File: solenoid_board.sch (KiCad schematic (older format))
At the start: 38 parts, among them J1 Screw_Terminal_01x02, J10 Screw_Terminal_01x02, J11 Screw_Terminal_01x02, J12 Screw_Terminal_01x06, J13 Conn_01x01_Male, J14 Screw_Terminal_01x06, J2 MCU_LEFT_LEGS, J3 MCU_RIGHT_LEGS, J4 RJ45, J5 RJ45, J6 Screw_Terminal_01x06, J7 Screw_Terminal_01x02, J8 Screw_Terminal_01x02, J9 Screw_Terminal_01x02, Q1 PHP79NQ08LT, Q2 PHP79NQ08LT, Q3 PHP79NQ08LT, Q4 PHP79NQ08LT, Q5 PHP79NQ08LT, Q6 PHP79NQ08LT, U1 CDSOT23-SM712, U4 SN65HVD72DR, U5 74HC165, U6 74HC165

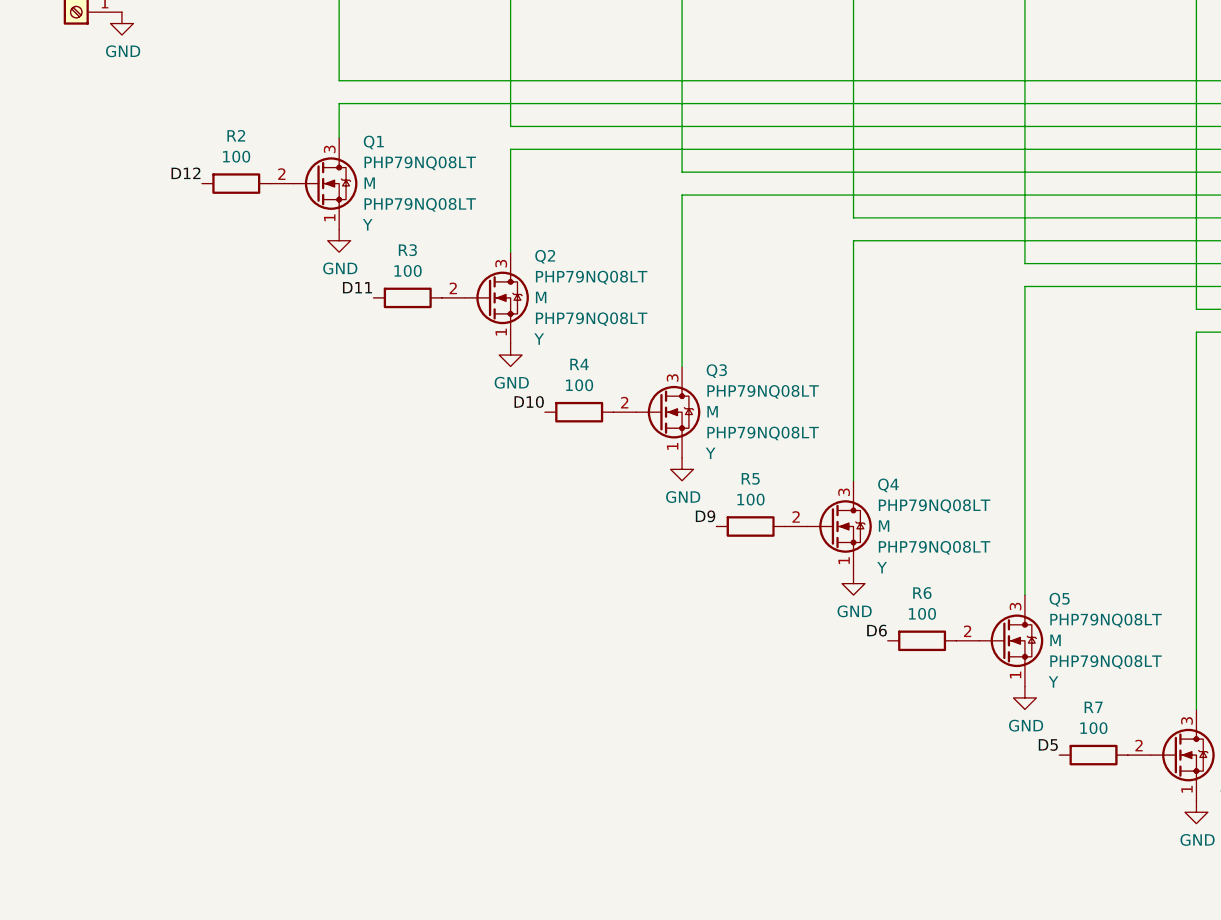
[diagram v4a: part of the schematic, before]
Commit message: Laid about half the wire. Next Step, lay out the wires for the digital electronics
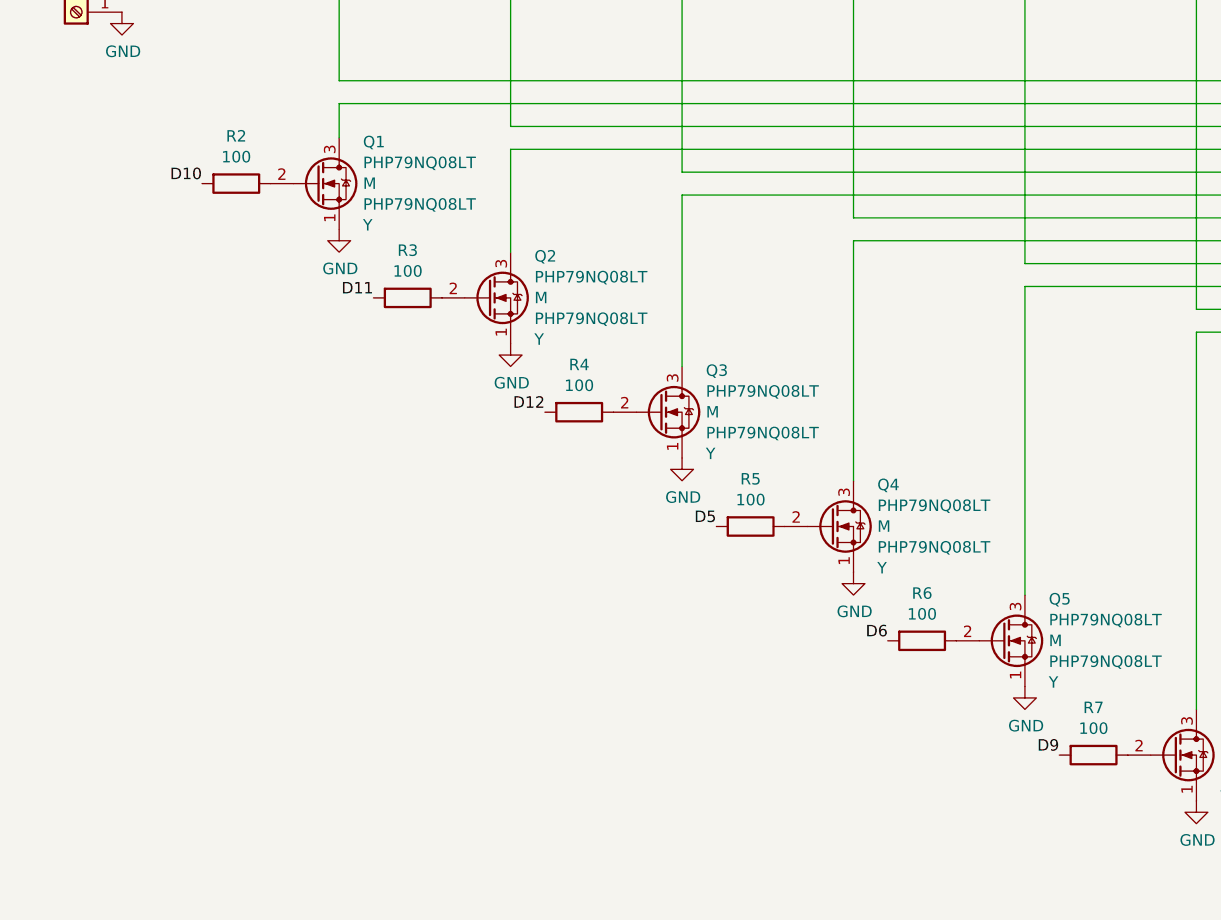
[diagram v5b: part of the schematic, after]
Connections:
- net D10: now also R2.2; no longer R4.2
- net D12: now also R4.2; no longer R2.2
- net D5: now also R5.2; no longer R7.2
- net D9: now also R7.2; no longer R5.2
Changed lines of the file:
@@
 $EndComp
 Text Label 5150 1900 2    50   ~ 0
-D12
+D10
 $Comp
 L MOSFETs:PHP79NQ08LT Q1
@@
 D11
 Text Label 6650 2900 2    50   ~ 0
-D10
+D12
 Text Label 7400 3400 2    50   ~ 0
-D9
+D5
 Text Label 8150 3900 2    50   ~ 0
 D6
 Text Label 8900 4400 2    50   ~ 0
-D5
+D9
 Text Label 1250 6250 0    50   ~ 0
 INP0_0

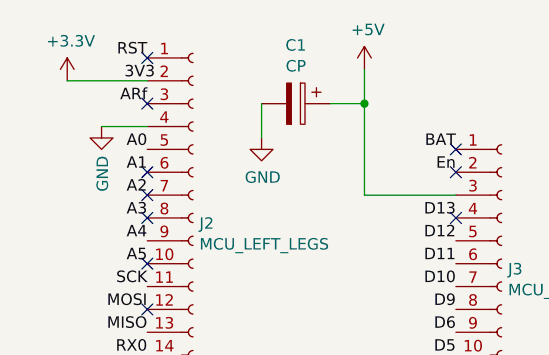
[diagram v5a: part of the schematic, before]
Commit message: Wired up the RS-485 Transciever
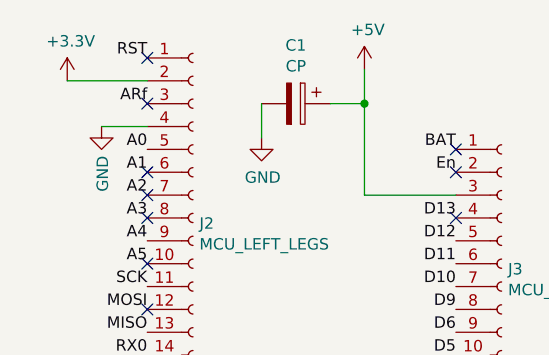
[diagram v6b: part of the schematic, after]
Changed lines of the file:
@@
 Text Label 1200 700  2    50   ~ 0
 RST
-Text Label 1100 800  0    50   ~ 0
-3V3
 Text Label 1200 900  2    50   ~ 0
 ARf

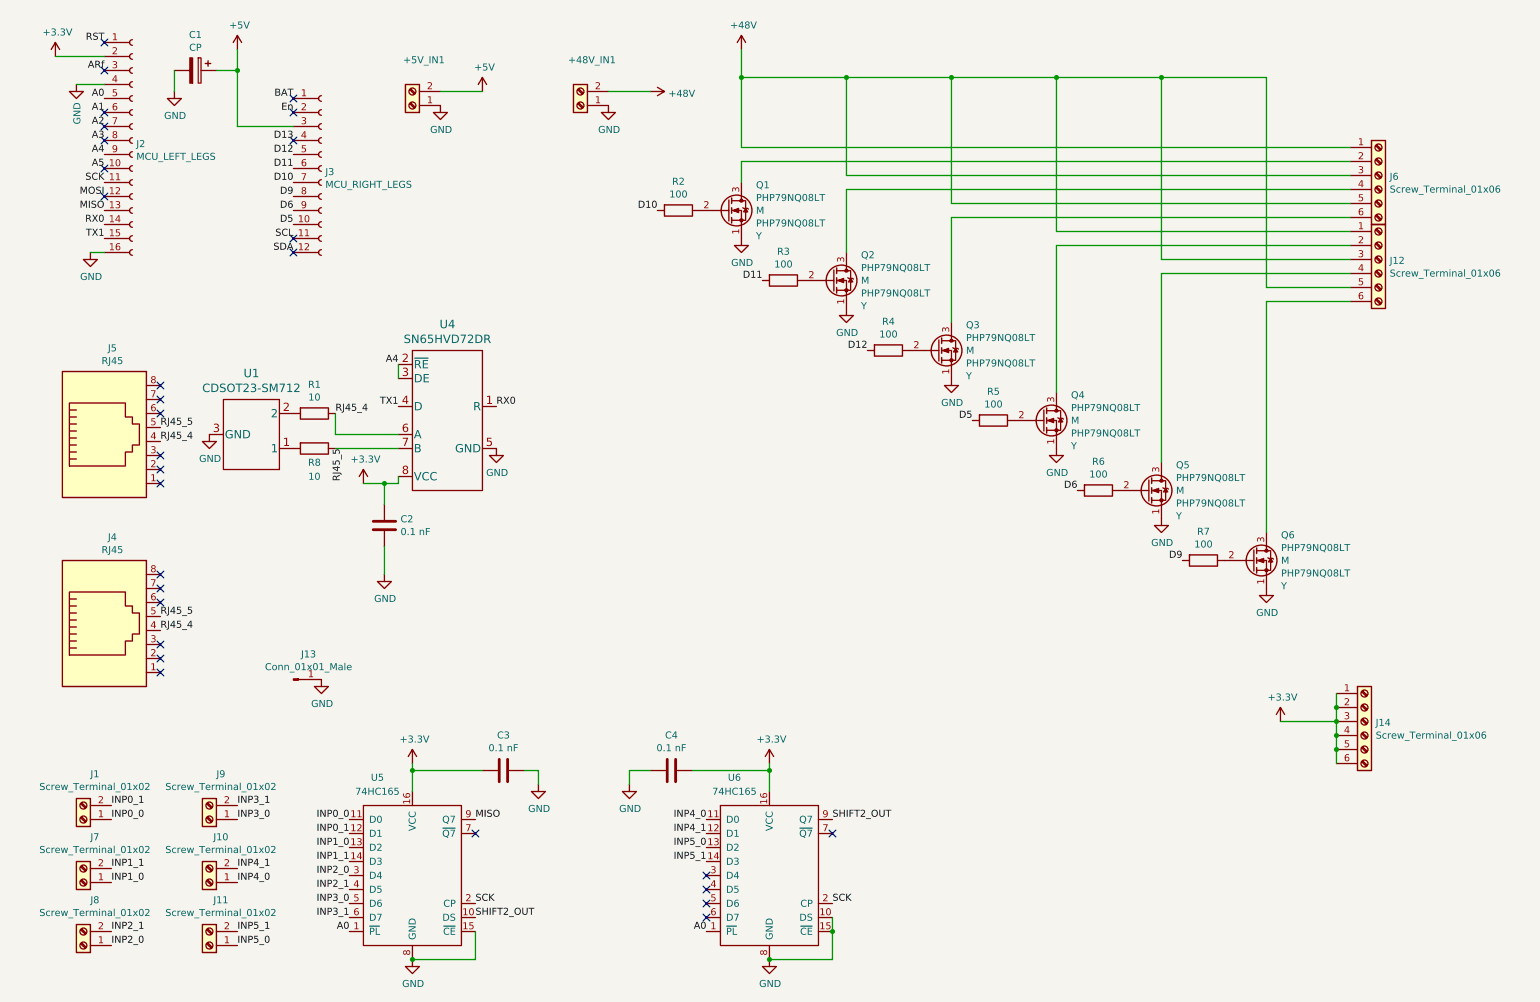
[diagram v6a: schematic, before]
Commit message: Change symbol names and place silk writing onto the board. Next Step: Order PCB
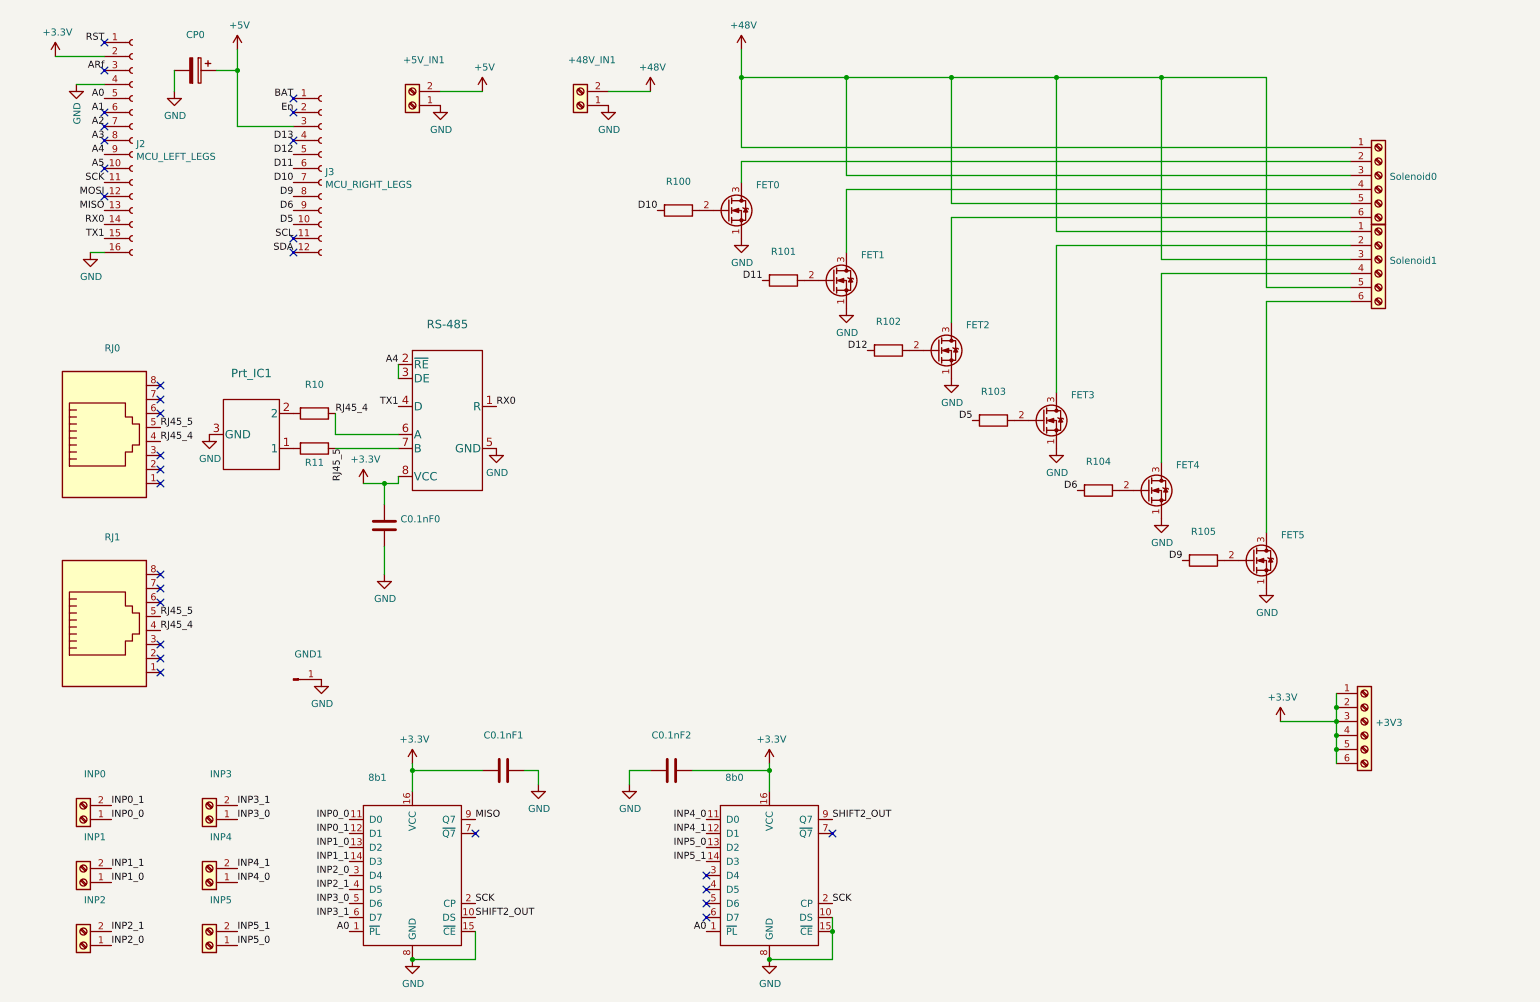
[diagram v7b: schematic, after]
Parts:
- renumbered J14 to +3V3, U6 to 8b0, U5 to 8b1, C2 to C0.1nF0, C3 to C0.1nF1, C4 to C0.1nF2, C1 to CP0, Q1 to FET0, Q2 to FET1, Q3 to FET2, Q4 to FET3, Q5 to FET4, Q6 to FET5, J13 to GND1, J1 to INP0, J7 to INP1, J8 to INP2, J9 to INP3, J10 to INP4, J11 to INP5, U1 to Prt_IC1, R1 to R10, R2 to R100, R3 to R101, R4 to R102, R5 to R103, R6 to R104, R7 to R105, R8 to R11, J5 to RJ0, J4 to RJ1, U4 to RS-485, J6 to Solenoid0, J12 to Solenoid1
